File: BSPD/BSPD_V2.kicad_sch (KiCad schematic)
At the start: 33 parts, among them J2 Conn_01x02_Socket, J3 Conn_01x02_Socket, J4 Conn_01x02_Socket, K1 Fujitsu_FTR-LYCA005x, Q1 AO3400A, Q2 AO3400A, Q3 NPN, Q4 AO3400A, Q5 NPN, U1 CD4001BM, U2 CD4001BM, U3 LM393, U5 LM393

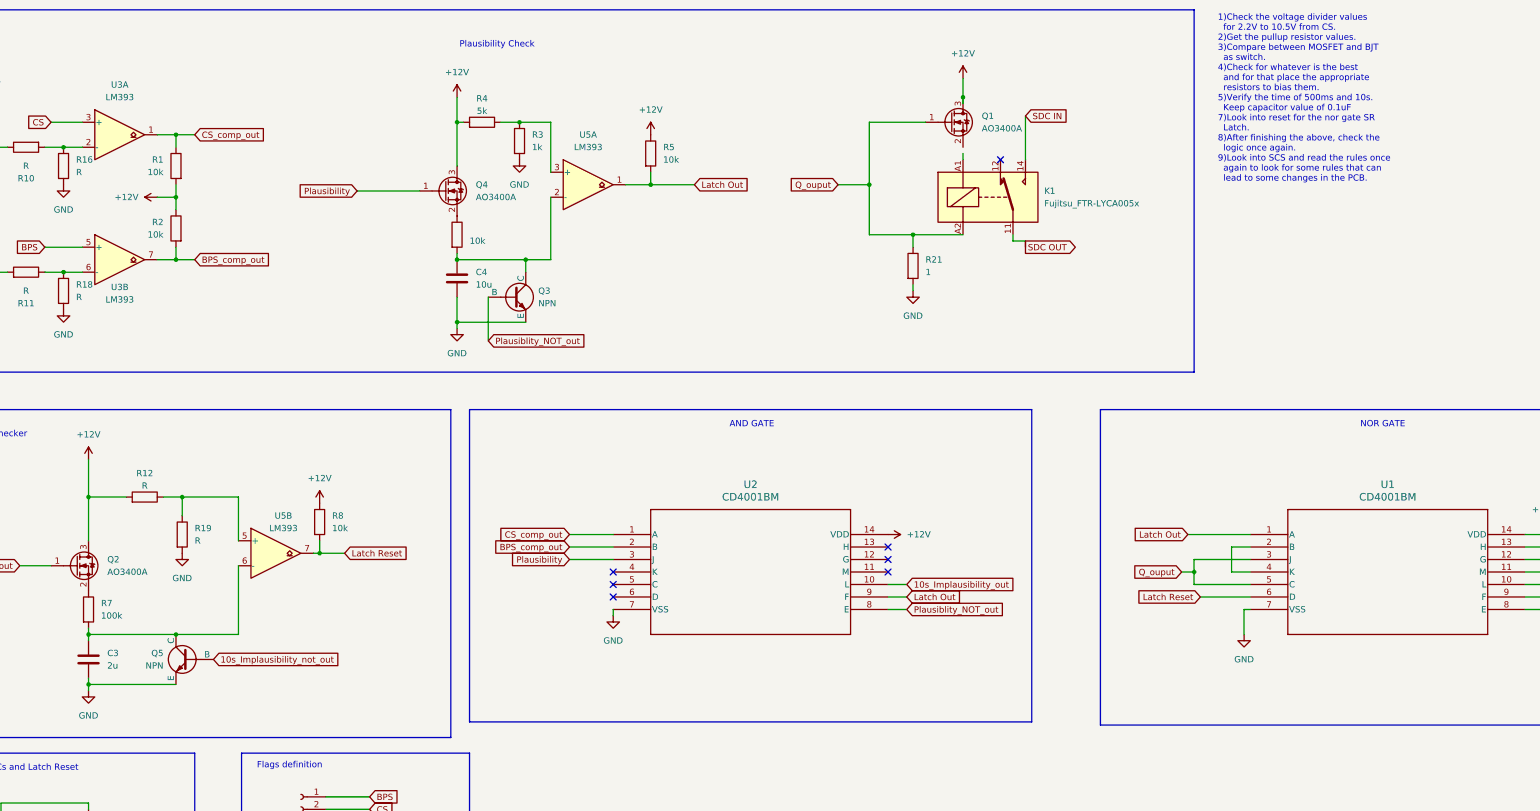
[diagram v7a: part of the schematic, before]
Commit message: Added the image of the schematic for better refernence
Added standard resistance values for the 500ms delay setup,
using the NPN transistor as a switch to discharge the capacitor
in ~2ms with a current of range between 0-10mA. This is well within
price and specs of the current BJTs.

Also looked into MOSFETs, but they didn't discharge the capacitor
at all(NMOS and PMOS).

NPN transistor still has to be figured out but that should be
a piece of cake hopefully..

Also, changed voltage divider values to standard, aims for
~11.7V and the resistor at the tail end of the BJT also helps
in controlling the amount of current the NPN transistor needs
to flow through it.
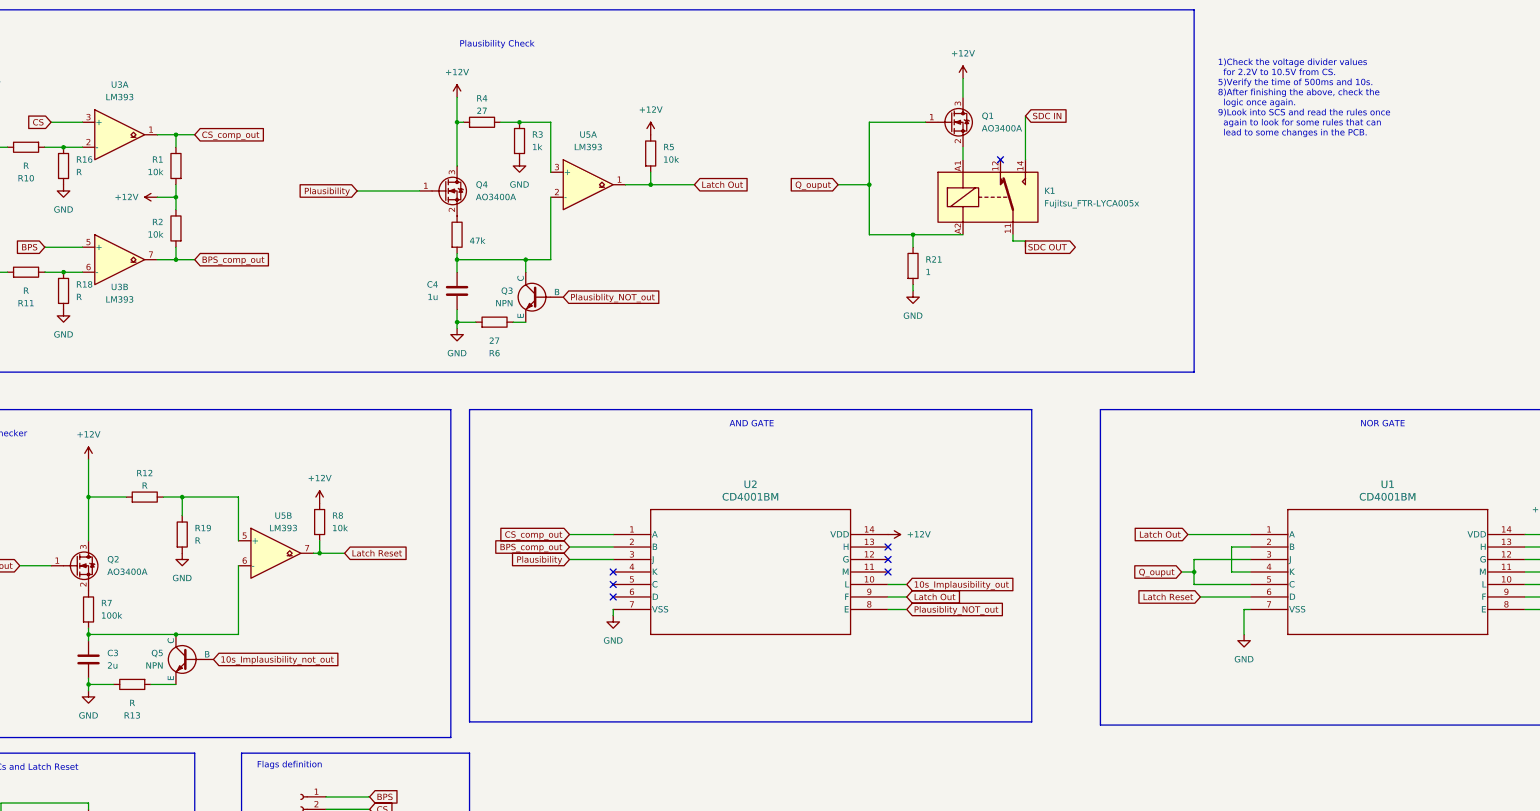
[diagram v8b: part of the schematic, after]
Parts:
- added R13: R, symbol Device:R
- added R6: 27, symbol Device:R
- C4: value 10u -> 1u
- R14: value 10k -> 47k
- R4: value 5k -> 27
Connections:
- net GND: now also R13.1, R6.2; no longer Q3.3 (E), Q5.3 (E)
- net at K1.A1: now also Q1.2 (S)
- new net: Q5.3 (E), R13.2
- new net: Q3.3 (E), R6.1
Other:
- note added: "1)Check the voltage divider values for 2.2V to 10.5V from CS. 5)Verify the time of 500ms and 10s. 8)After finishing the above, check the logic once again. 9)Look into SCS and read the rules once again to look for some rules that can lead to some changes in the PCB."
- note removed: "1)Check the voltage divider values for 2.2V to 10.5V from CS. 2)Get the pullup resistor values. 3)Compare between MOSFET and BJT as switch. 4)Check for whatever is the best and for that place the appropriate resistors to bias them. 5)Verify the time of 500ms and 10s. Keep capacitor value of 0.1uF 7)Look into reset for the nor gate SR Latch. 8)After finishing the above, check the logic once again.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"
- moved on the sheet: C4, Q3
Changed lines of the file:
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@@
 	)
 	(junction
-		(at 250.19 50.8)
-		(diameter 0)
-		(color 0 0 0 0)
-	)
-	(junction
 		(at 67.31 60.96)
 		(diameter 0)
@@
 	(wire
 		(pts
-			(xy 147.32 91.44) (xy 147.32 96.52)
+			(xy 147.32 93.98) (xy 147.32 96.52)
 		)
 		(stroke
@@
 	(wire
 		(pts
+			(xy 147.32 96.52) (xy 151.13 96.52)
+		)
+		(stroke
+			(width 0)
+			(type default)
+		)
+	)
+	(wire
+		(pts
 			(xy 93.98 58.42) (xy 90.17 58.42)
 		)
@@
 	(wire
 		(pts
-			(xy 250.19 50.8) (xy 250.19 52.07)
-		)
-		(stroke
-			(width 0)
-			(type default)
-		)
-	)
-	(wire
-		(pts
 			(xy 91.44 132.08) (xy 102.87 132.08)
 		)
@@
 	(wire
 		(pts
-			(xy 369.57 152.4) (xy 369.57 154.94)
+			(xy 250.19 60.96) (xy 250.19 63.5)
 		)
 		(stroke
@@
 	(wire
 		(pts
-			(xy 90.17 81.28) (xy 90.17 83.82)
+			(xy 369.57 152.4) (xy 369.57 154.94)
 		)
 		(stroke
@@
 	(wire
 		(pts
-			(xy 238.76 152.4) (xy 234.95 152.4)
+			(xy 90.17 81.28) (xy 90.17 83.82)
 		)
 		(stroke
@@
 	(wire
 		(pts
-			(xy 147.32 83.82) (xy 161.29 83.82)
+			(xy 238.76 152.4) (xy 234.95 152.4)
 		)
 		(stroke
@@
 	(wire
 		(pts
-			(xy 161.29 96.52) (xy 147.32 96.52)
+			(xy 147.32 83.82) (xy 161.29 83.82)
 		)
 		(stroke
@@
 	(wire
 		(pts
-			(xy 40.64 213.36) (xy 40.64 215.9)
+			(xy 85.09 170.18) (xy 90.17 170.18)
 		)
 		(stroke
@@
 	(wire
 		(pts
-			(xy 250.19 46.99) (xy 250.19 50.8)
+			(xy 40.64 213.36) (xy 40.64 215.9)
 		)
 		(stroke
@@
 	(wire
 		(pts
-			(xy 238.76 149.86) (xy 234.95 149.86)
+			(xy 250.19 46.99) (xy 250.19 50.8)
 		)
 		(stroke
@@
 	(wire
 		(pts
-			(xy 369.57 144.78) (xy 364.49 144.78)
+			(xy 238.76 149.86) (xy 234.95 149.86)
 		)
 		(stroke
@@
 	(wire
 		(pts
-			(xy 49.53 213.36) (xy 54.61 213.36)
+			(xy 369.57 144.78) (xy 364.49 144.78)
 		)
 		(stroke
@@
 	(wire
 		(pts
-			(xy 63.5 81.28) (xy 71.12 81.28)
+			(xy 49.53 213.36) (xy 54.61 213.36)
 		)
 		(stroke
@@
 	(wire
 		(pts
-			(xy 153.67 91.44) (xy 153.67 100.33)
+			(xy 63.5 81.28) (xy 71.12 81.28)
 		)
 		(stroke
@@
 	(wire
 		(pts
-			(xy 250.19 62.23) (xy 250.19 63.5)
+			(xy 186.69 68.58) (xy 195.58 68.58)
 		)
 		(stroke
@@
 	(wire
 		(pts
-			(xy 186.69 68.58) (xy 195.58 68.58)
+			(xy 90.17 68.58) (xy 90.17 71.12)
 		)
 		(stroke
@@
 	(wire
 		(pts
-			(xy 90.17 68.58) (xy 90.17 71.12)
+			(xy 170.18 139.7) (xy 179.07 139.7)
 		)
 		(stroke
@@
 	(wire
 		(pts
-			(xy 170.18 139.7) (xy 179.07 139.7)
+			(xy 90.17 83.82) (xy 93.98 83.82)
 		)
 		(stroke
@@
 	(wire
 		(pts
-			(xy 90.17 83.82) (xy 93.98 83.82)
+			(xy 147.32 86.36) (xy 147.32 83.82)
 		)
 		(stroke
@@
 	(wire
 		(pts
-			(xy 72.39 170.18) (xy 90.17 170.18)
+			(xy 72.39 170.18) (xy 77.47 170.18)
 		)
 		(stroke
@@
 	(wire
 		(pts
+			(xy 158.75 96.52) (xy 161.29 96.52)
+		)
+		(stroke
+			(width 0)
+			(type default)
+		)
+	)
+	(wire
+		(pts
 			(xy 40.64 213.36) (xy 49.53 213.36)
 		)
@@
 		)
 	)
-	(text "1)Check the voltage divider values \n  for 2.2V to 10.5V from CS.\n2)Get the pullup resistor values.\n3)Compare between MOSFET and BJT \n  as switch.\n4)Check for whatever is the best \n  and for that place the appropriate \n  resistors to bias them.\n5)Verify the time of 500ms and 10s. \n  Keep capacitor value of 0.1uF\n7)Look into reset for the nor gate SR\n  Latch.\n8)After finishing the above, check the\n  logic once again.\n9)Look into SCS and read the rules once\n  again to look for some rules that can\n  lead to some changes in the PCB.\n"
+	(text "1)Check the voltage divider values \n  for 2.2V to 10.5V from CS.\n5)Verify the time of 500ms and 10s. \n8)After finishing the above, check the\n  logic once again.\n9)Look into SCS and read the rules once\n  again to look for some rules that can\n  lead to some changes in the PCB.\n"
 		(exclude_from_sim no)
 		(at 302.006 51.054 0)
@@
 	(global_label "Plausiblity_NOT_out"
 		(shape input)
-		(at 153.67 100.33 0)
+		(at 168.91 91.44 0)
 		(fields_autoplaced yes)
 		(effects
@@
 		)
 		(property "Intersheetrefs" "${INTERSHEET_REFS}"
-			(at 175.2211 100.33 0)
+			(at 190.4611 91.44 0)
 			(effects
 				(font
@@
 			)
 		)
-		(property "Value" "5k"
+		(property "Value" "27"
 			(at 152.4 53.594 90)
 			(effects
@@
 			)
 		)
-		(property "Value" "10k"
+		(property "Value" "47k"
 			(at 149.86 80.0099 0)
 			(effects
@@
 	)
 	(symbol
+		(lib_id "Device:R")
+		(at 81.28 170.18 90)
+		(mirror x)
+		(unit 1)
+		(exclude_from_sim no)
+		(in_bom yes)
+		(on_board yes)
+		(dnp no)
+		(property "Reference" "R13"
+			(at 81.28 176.53 90)
+			(effects
+				(font
+					(size 1.27 1.27)
+				)
+			)
+		)
+		(property "Value" "R"
+			(at 81.28 173.99 90)
+			(effects
+				(font
+					(size 1.27 1.27)
+				)
+			)
+		)
+		(property "Footprint" ""
+			(at 81.28 168.402 90)
+			(effects
+				(font
+					(size 1.27 1.27)
+				)
+				(hide yes)
+			)
+		)
+		(property "Datasheet" "~"
+			(at 81.28 170.18 0)
+			(effects
+				(font
+					(size 1.27 1.27)
+				)
+				(hide yes)
+			)
+		)
+		(property "Description" "Resistor"
+			(at 81.28 170.18 0)
+			(effects
+				(font
+					(size 1.27 1.27)
+				)
+				(hide yes)
+			)
+		)
+		(pin "2"
+		)
+		(pin "1"
+		)
+		(instances
+			(project ""
+				(path "/d92b65b7-5ac6-4942-9c7f-8311f0326af7"
+					(reference "R13")
+					(unit 1)
+				)
+			)
+		)
+	)
+	(symbol
 		(lib_id "Transistor_FET:AO3400A")
 		(at 144.78 69.85 0)
@@
 	(symbol
 		(lib_id "Simulation_SPICE:NPN")
-		(at 158.75 91.44 0)
+		(at 163.83 91.44 0)
+		(mirror y)
 		(unit 1)
 		(exclude_from_sim no)
@@
 		(on_board yes)
 		(dnp no)
-		(fields_autoplaced yes)
 		(property "Reference" "Q3"
-			(at 163.83 90.1699 0)
+			(at 158.75 90.1699 0)
 			(effects
 				(font
@@
 		)
 		(property "Value" "NPN"
-			(at 163.83 92.7099 0)
+			(at 158.75 92.7099 0)
 			(effects
 				(font
@@
 		)
 		(property "Footprint" ""
-			(at 222.25 91.44 0)
+			(at 100.33 91.44 0)
 			(effects
 				(font
@@
 		)
 		(property "Datasheet" "https://ngspice.sourceforge.io/docs/ngspice-html-manual/manual.xhtml#cha_BJTs"
-			(at 222.25 91.44 0)
+			(at 100.33 91.44 0)
 			(effects
 				(font
@@
 		)
 		(property "Description" "Bipolar transistor symbol for simulation only, substrate tied to the emitter"
-			(at 158.75 91.44 0)
+			(at 163.83 91.44 0)
 			(effects
 				(font
@@
 		)
 		(property "Sim.Device" "NPN"
-			(at 158.75 91.44 0)
+			(at 163.83 91.44 0)
 			(effects
 				(font
@@
 		)
 		(property "Sim.Type" "GUMMELPOON"
-			(at 158.75 91.44 0)
+			(at 163.83 91.44 0)
 			(effects
 				(font
@@
 		)
 		(property "Sim.Pins" "1=C 2=B 3=E"
-			(at 158.75 91.44 0)
+			(at 163.83 91.44 0)
 			(effects
 				(font
@@
 	(symbol
 		(lib_id "Device:C")
-		(at 147.32 87.63 0)
+		(at 147.32 90.17 0)
+		(mirror y)
 		(unit 1)
 		(exclude_from_sim no)
@@
 		(on_board yes)
 		(dnp no)
-		(fields_autoplaced yes)
 		(property "Reference" "C4"
-			(at 151.13 86.3599 0)
+			(at 143.51 88.8999 0)
 			(effects
 				(font
@@
 			)
 		)
-		(property "Value" "10u"
-			(at 151.13 88.8999 0)
+		(property "Value" "1u"
+			(at 143.51 91.4399 0)
 			(effects
 				(font
@@
 		)
 		(property "Footprint" ""
-			(at 148.2852 91.44 0)
+			(at 146.3548 93.98 0)
 			(effects
 				(font
@@
 		)
 		(property "Datasheet" "~"
-			(at 147.32 87.63 0)
+			(at 147.32 90.17 0)
 			(effects
 				(font
@@
 		)
 		(property "Description" "Unpolarized capacitor"
-			(at 147.32 87.63 0)
+			(at 147.32 90.17 0)
 			(effects
 				(font
@@
 					(unit 1)
 				)
+			)
+		)
+	)
+	(symbol
+		(lib_id "Device:R")
+		(at 154.94 96.52 270)
+		(mirror x)
+		(unit 1)
+		(exclude_from_sim no)
+		(in_bom yes)
+		(on_board yes)
+		(dnp no)
+		(property "Reference" "R6"
+			(at 154.94 102.87 90)
+			(effects
+				(font
+					(size 1.27 1.27)
+				)
+			)
+		)
+		(property "Value" "27"
+			(at 154.94 100.33 90)
+			(effects
+				(font
+					(size 1.27 1.27)
+				)
+			)
+		)
+		(property "Footprint" ""
+			(at 154.94 98.298 90)
+			(effects
+				(font
+					(size 1.27 1.27)
+				)
+				(hide yes)
+			)
+		)
+		(property "Datasheet" "~"
+			(at 154.94 96.52 0)
+			(effects
+				(font
+					(size 1.27 1.27)
+				)
+				(hide yes)
+			)
+		)
+		(property "Description" "Resistor"
+			(at 154.94 96.52 0)
+			(effects
+				(font
+					(size 1.27 1.27)
+				)
+				(hide yes)
+			)
+		)
+		(pin "1"
+		)
+		(pin "2"
+		)
+		(instances
+			(project ""
+				(path "/d92b65b7-5ac6-4942-9c7f-8311f0326af7"
+					(reference "R6")
+					(unit 1)
+				)
